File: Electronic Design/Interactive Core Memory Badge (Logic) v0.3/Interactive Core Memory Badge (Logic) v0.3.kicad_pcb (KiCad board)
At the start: 2 copper layers, 85.2 x 170.1 mm, 126 parts, among them J1 SSW-116-22-F-S-VS‎, J10 Conn_01x08_Female, J11 Conn_01x08_Female, J12 Conn_01x08_Female, J13 Conn_01x08_Female, J2 SSW-116-22-F-S-VS‎, J3 BM03B-PASS-1-TFT__LF__SN_, J4 Conn_01x02_Male, J5 SSW-104-22-L-S-VS, J6 Conn_01x08_Female, J7 Conn_01x04_Male, J8 Conn_01x08_Female, J9 TSM-106-03-T-DV‎, Q1 IRLML6344TRPBF, Q10 MMBT4401LT1G, Q11 MMBT4403LT1G, Q12 MMBT4401LT1G, Q13 MMBT4403LT1G, Q14 MMBT4401LT1G, Q15 MMBT4403LT1G, Q16 MMBT4401LT1G, Q17 MMBT4403LT1G, Q18 MMBT4401LT1G, Q19 MMBT4403LT1G, Q2 MMBT4403LT1G, Q20 MMBT4401LT1G, Q21 MMBT4403LT1G, Q22 MMBT4401LT1G, Q3 MMBT4401LT1G, Q4 MMBT4401LT1G, Q5 MMBT4403LT1G, Q6 MMBT4401LT1G, Q7 MMBT4403LT1G, Q8 MMBT4401LT1G, Q9 MMBT4403LT1G, SW1 JS102011SAQN, U1 LD1117S33TR_SOT223, U10 M24C01-RMN, U2 Teensy-LC, U3 LM393, U4 74HC02, U5 MCP23017_SO, U6 MCP23017_SO, U7 SN74LV1T125DBVR, U8 74AC04, U9 74AC04, X1 SAO_conn_SFH11-NBPC-D03-ST-BK, X2 SAO_conn_SFH11-NBPC-D03-ST-BK, X3 SAO_conn_SFH11-NBPC-D03-ST-BK

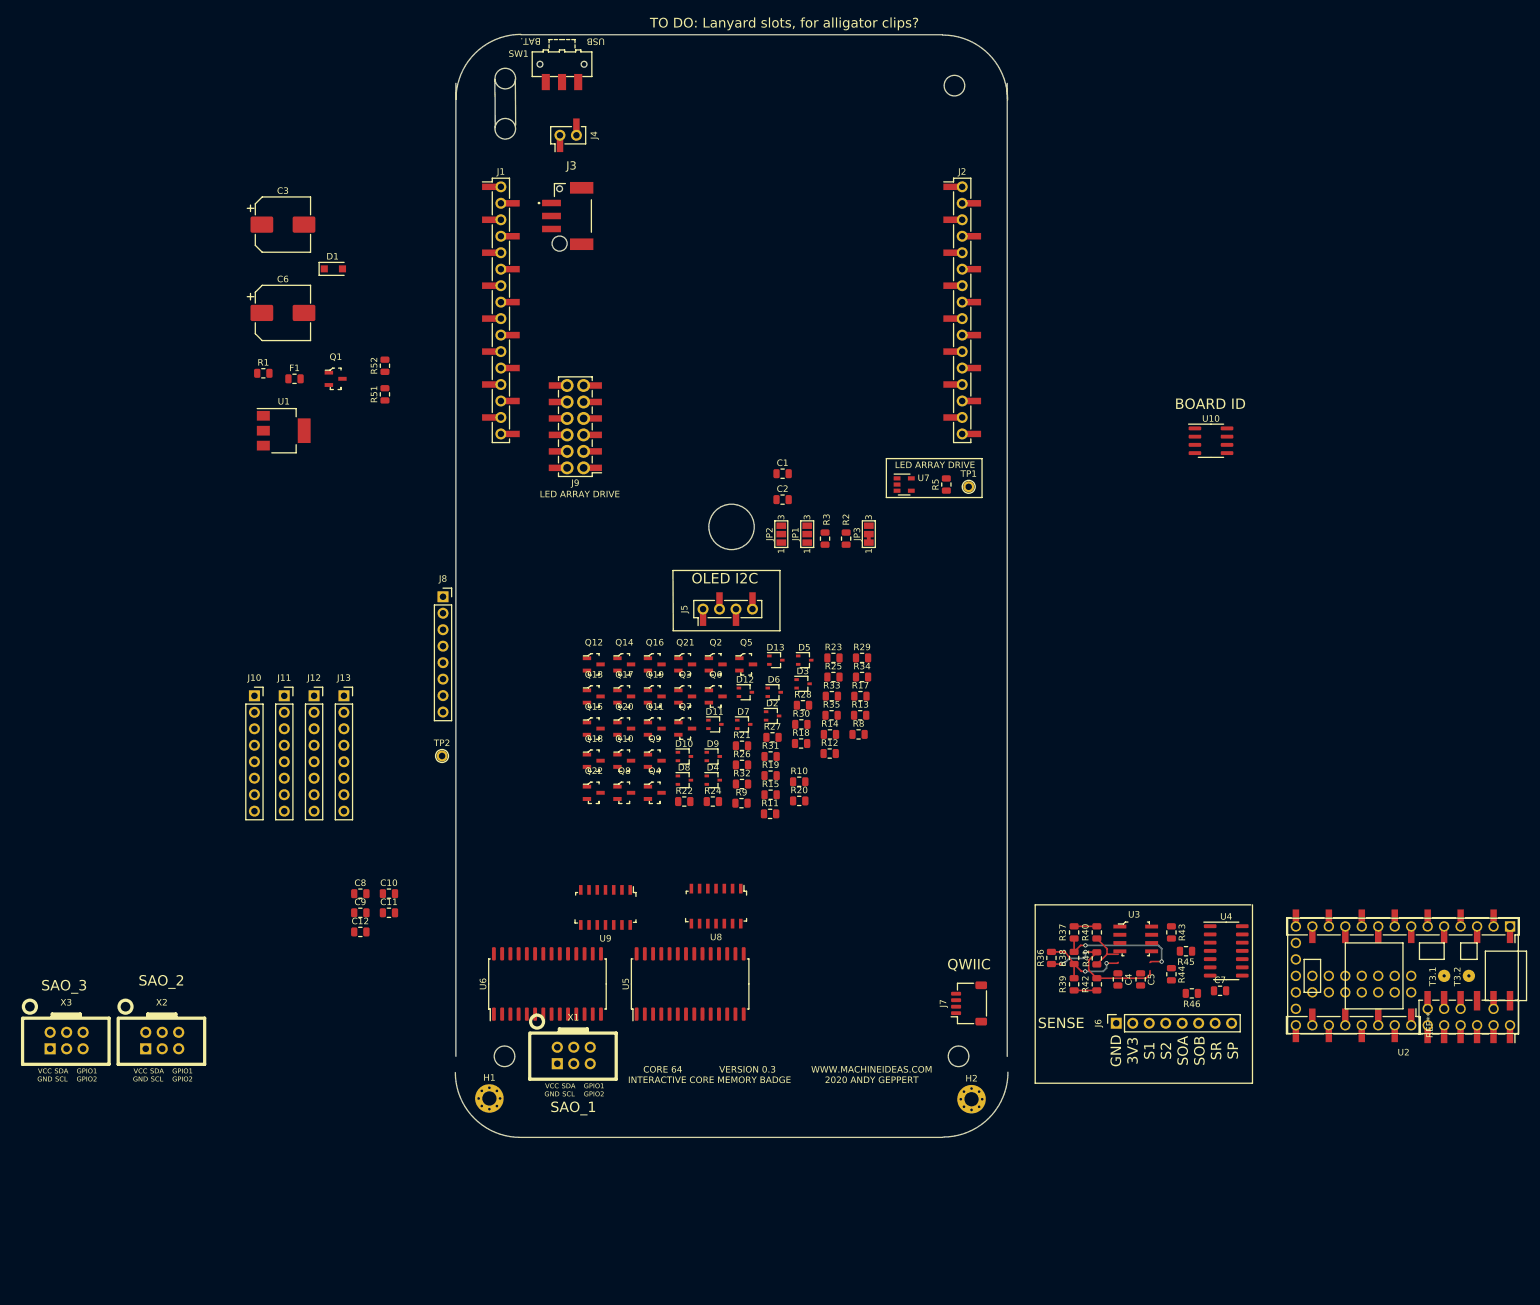
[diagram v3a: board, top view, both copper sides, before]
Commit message: Board layout, PDFs for review
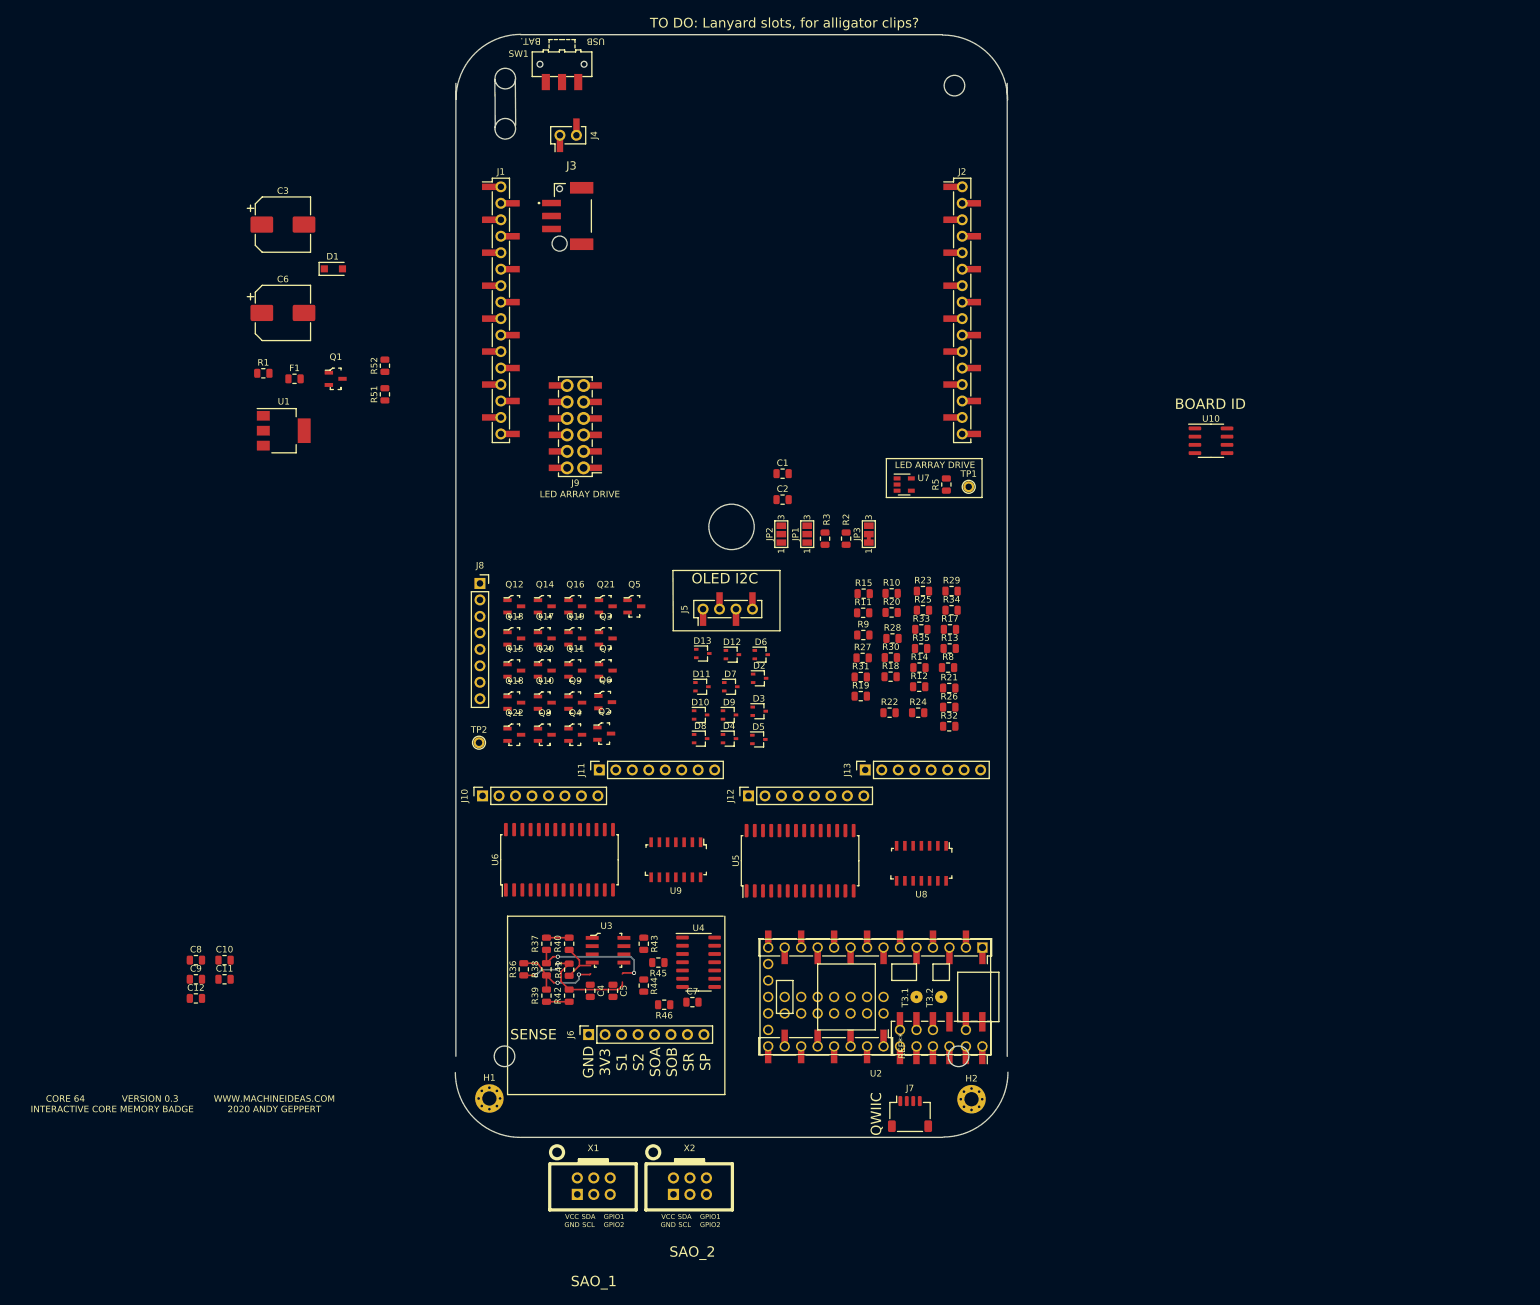
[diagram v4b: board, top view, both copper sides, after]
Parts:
- removed X3: SAO_conn_SFH11-NBPC-D03-ST-BK, badgelife_sao_v169bis:Badgelife-SAOv169-BADGE-2x3
- moved X2 84.4 mm to (-6.47, 135.0)
- moved U2 81.4 mm to (22.2, 105.8)
- moved R46 81.4 mm to (-10.4, 107.0)
- moved C4 81.4 mm to (-21.8, 104.9)
- moved C5 81.4 mm to (-18.3, 104.9)
- moved C7 81.4 mm to (-6.04, 106.7)
- moved J6 81.4 mm to (-22.0, 111.7)
- moved R36 81.4 mm to (-32.0, 101.6)
- moved R37 81.4 mm to (-28.5, 97.7)
- moved R38 81.4 mm to (-28.5, 101.6)
- moved R39 81.4 mm to (-28.5, 105.7)
- moved R40 81.4 mm to (-25.0, 97.7)
- moved R41 81.4 mm to (-25.0, 101.7)
- moved R42 81.4 mm to (-25.0, 105.7)
- moved R43 81.4 mm to (-13.5, 97.7)
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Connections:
- net BOARD_ID1 renamed SPARE_3
- net BOARD_ID2 renamed SPARE_4
- net BOARD_ID3 renamed SPARE_5
- J2 pad 16: Net-(J2-Pad16) -> SAO3_GPIO2
- U2 pad 10: Net-(U2-Pad10) -> SENSE_OUT_B
- U2 pad 23: Net-(U2-Pad23) -> SAO3_GPIO2
- U2 pad 29: SAO3_GPIO2 -> Net-(U2-Pad29)
- U2 pad 30: SAO3_GPIO1 -> Net-(U2-Pad30)
- U2 pad 9: Net-(U2-Pad9) -> SENSE_OUT_A
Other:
- board text removed: "SAO_3"

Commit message: Schematic review tweaks
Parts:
- turned J4 to 0 degrees
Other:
- board text added: "+"
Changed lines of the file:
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@@
   (general
     (thickness 1.6)
-    (drawings 56)
+    (drawings 58)
     (tracks 45)
     (zones 0)
@@
     (aux_axis_origin 0 0)
     (grid_origin 94.615 196.85)
-    (visible_elements FFFFE7FF)
+    (visible_elements FFFFEFFF)
     (pcbplotparams
       (layerselection 0x010f0_ffffffff)
@@
   )
   (module Connector_PinSocket_2.54mm:PinSocket_1x02_P2.54mm_Vertical_SMD_Pin1Left (layer F.Cu)
-    (at -25.185 -27 90)
+    (at -25.185 -27)
     (descr "surface-mounted straight socket strip, 1x02, 2.54mm pitch, single row, style 1 (pin 1 left) (https://cdn.harwin.com/pdfs/M20-786.pdf), script generated")
     (tags "Surface mounted socket strip SMD 1x02 2.54mm single row style1 pin1 left")
     (attr smd)
-    (fp_text reference J4 (at 0 4 90) (layer F.SilkS)
+    (fp_text reference J4 (at -4.2 0.85) (layer F.SilkS)
       (effects (font (size 1 1) (thickness 0.15)))
     )
-    (fp_text value Conn_01x02_Male (at 0 4.14 90) (layer F.Fab)
+    (fp_text value Conn_01x02_Male (at 0 4.14) (layer F.Fab)
       (effects (font (size 1 1) (thickness 0.15)))
     )
-    (fp_text user %R (at 0 0) (layer F.Fab)
+    (fp_text user %R (at 0 0 90) (layer F.Fab)
       (effects (font (size 1 1) (thickness 0.15)))
     )
@@
     (fp_line (start 1.33 -2.7) (end 1.33 0.51) (layer F.SilkS) (width 0.12))
     (fp_line (start -1.33 -2.7) (end 1.33 -2.7) (layer F.SilkS) (width 0.12))
-    (pad 2 thru_hole circle (at 0 1.27 90) (size 1.7 1.7) (drill 1) (layers *.Cu *.Mask)
+    (pad 2 thru_hole circle (at 0 1.27) (size 1.7 1.7) (drill 1) (layers *.Cu *.Mask)
       (net 3 -BATT))
-    (pad 1 thru_hole circle (at 0 -1.27 90) (size 1.7 1.7) (drill 1) (layers *.Cu *.Mask)
+    (pad 1 thru_hole circle (at 0 -1.27) (size 1.7 1.7) (drill 1) (layers *.Cu *.Mask)
       (net 115 +BATT))
-    (pad 2 smd rect (at 1.65 1.27 90) (size 1.9 1) (layers F.Cu F.Paste F.Mask)
+    (pad 2 smd rect (at 1.65 1.27) (size 1.9 1) (layers F.Cu F.Paste F.Mask)
       (net 3 -BATT))
-    (pad 1 smd rect (at -1.65 -1.27 90) (size 1.9 1) (layers F.Cu F.Paste F.Mask)
+    (pad 1 smd rect (at -1.65 -1.27) (size 1.9 1) (layers F.Cu F.Paste F.Mask)
       (net 115 +BATT))
     (model ${KISYS3DMOD}/Connector_PinSocket_2.54mm.3dshapes/PinSocket_1x02_P2.54mm_Vertical_SMD_Pin1Left.wrl
@@
     (descr "BM03B-PASS-1-TFT (LF)(SN)-3")
     (tags Connector)
-    (fp_text reference J3 (at 7.75 0 180) (layer F.SilkS)
+    (fp_text reference J3 (at 7.6 -3.7 180) (layer F.SilkS)
       (effects (font (size 1.27 1.27) (thickness 0.254)))
     )
@@
       (net 125 "SAO2_GPIO1(TX)"))
   )
+  (gr_text + (at -29.385 -19.15) (layer F.SilkS)
+    (effects (font (size 1 1) (thickness 0.15)))
+  )
+  (gr_text + (at -29.385 -28.15) (layer F.SilkS)
+    (effects (font (size 1 1) (thickness 0.15)))
+  )
   (gr_text BAT. (at -30.985 -41.5 180) (layer F.SilkS)

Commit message: I2C address updates
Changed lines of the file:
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@@
       (effects (font (size 0.75 0.75) (thickness 0.15)))
     )
-    (fp_text user VCC (at -3.29 4.731) (layer F.SilkS)
+    (fp_text user 3V3 (at -3.29 4.731) (layer F.SilkS)
       (effects (font (size 0.75 0.75) (thickness 0.15)))
     )
@@
       (effects (font (size 1 1) (thickness 0.15)))
     )
-    (fp_text user VCC (at -3.29 4.731) (layer F.SilkS)
+    (fp_text user 3V3 (at -3.29 4.731) (layer F.SilkS)
       (effects (font (size 0.75 0.75) (thickness 0.15)))
     )

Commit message: Schematic refinement
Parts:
- removed TP1: LED_MATRIX, TestPoint:TestPoint_THTPad_D1.7mm_Drill1.0mm
- removed TP2: VMEM, TestPoint:TestPoint_THTPad_D1.7mm_Drill1.0mm
- added J14: Conn_01x08_Female, Connector_PinSocket_2.54mm:PinSocket_1x08_P2.54mm_Vertical, F.Cu at (50.3, 73.7)
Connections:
- net LED_MATRIX_+VSW renamed LED_MATRIX_+VSW_SIG
- net LED_MATRIX_3V3 renamed LED_MATRIX_3V3_SIG
- J1 pad 11: 3V3_100mA -> 3V3_800mA
- R52 pad 2: -BATT -> TEENSY_GND
- U10 pad 1: TEENSY_GND -> 3V3_800mA
- U10 pad 2: TEENSY_GND -> 3V3_800mA
- U10 pad 3: TEENSY_GND -> 3V3_800mA
- U2 pad 10: SENSE_OUT_B -> SENSE_OUT_A
- U2 pad 11: SAO2_GPIO2(RX) -> SENSE_OUT_B
- U2 pad 12: SAO2_GPIO1(TX) -> SD_CS
- U2 pad 13: Net-(U2-Pad13) -> SD_DI
- U2 pad 14: Net-(U2-Pad14) -> SD_DO
- U2 pad 20: Net-(U2-Pad20) -> SD_CLK
- U2 pad 21: Net-(U2-Pad21) -> SD_CD
- U2 pad 8: Net-(U2-Pad8) -> SAO2_GPIO2(RX)
- U2 pad 9: SENSE_OUT_A -> SAO2_GPIO1(TX)
- U5 pad 16: TEENSY_GND -> 3V3_800mA
- U5 pad 17: TEENSY_GND -> 3V3_800mA
- U6 pad 16: TEENSY_GND -> 3V3_800mA
- U6 pad 17: TEENSY_GND -> 3V3_800mA
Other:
- board text added: "SD_CARD"
